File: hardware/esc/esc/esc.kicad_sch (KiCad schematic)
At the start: 17 parts, among them J1 JST SH 1.0mm, U10 TLV76733DRVR, U11 LMR51420YDDCR, U3 INA180B2

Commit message: redo layout and new board outline
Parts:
- C57, C58, C61, C62: footprint Capacitor_SMD:C_0603_1608Metric -> Capacitor_SMD:C_0402_1005Metric
- R21: footprint 3920:RES_3920R_1L00x_BRN -> Resistor_SMD:R_1206_3216Metric
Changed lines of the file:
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@@
 			)
 		)
-		(property "Footprint" "Capacitor_SMD:C_0603_1608Metric"
+		(property "Footprint" "Capacitor_SMD:C_0402_1005Metric"
 			(at 121.92 31.242 0)
 			(hide yes)
@@
 			)
 		)
-		(property "Footprint" "Capacitor_SMD:C_0603_1608Metric"
+		(property "Footprint" "Capacitor_SMD:C_0402_1005Metric"
 			(at 176.8348 49.53 0)
 			(hide yes)
@@
 			)
 		)
-		(property "Footprint" "Capacitor_SMD:C_0603_1608Metric"
+		(property "Footprint" "Capacitor_SMD:C_0402_1005Metric"
 			(at 90.4748 40.64 0)
 			(hide yes)
@@
 			)
 		)
-		(property "Footprint" "3920:RES_3920R_1L00x_BRN"
+		(property "Footprint" "Resistor_SMD:R_1206_3216Metric"
 			(at 27.432 35.56 90)
 			(hide yes)
@@
 			)
 		)
-		(property "Footprint" "Capacitor_SMD:C_0603_1608Metric"
+		(property "Footprint" "Capacitor_SMD:C_0402_1005Metric"
 			(at 212.3948 36.83 0)
 			(hide yes)

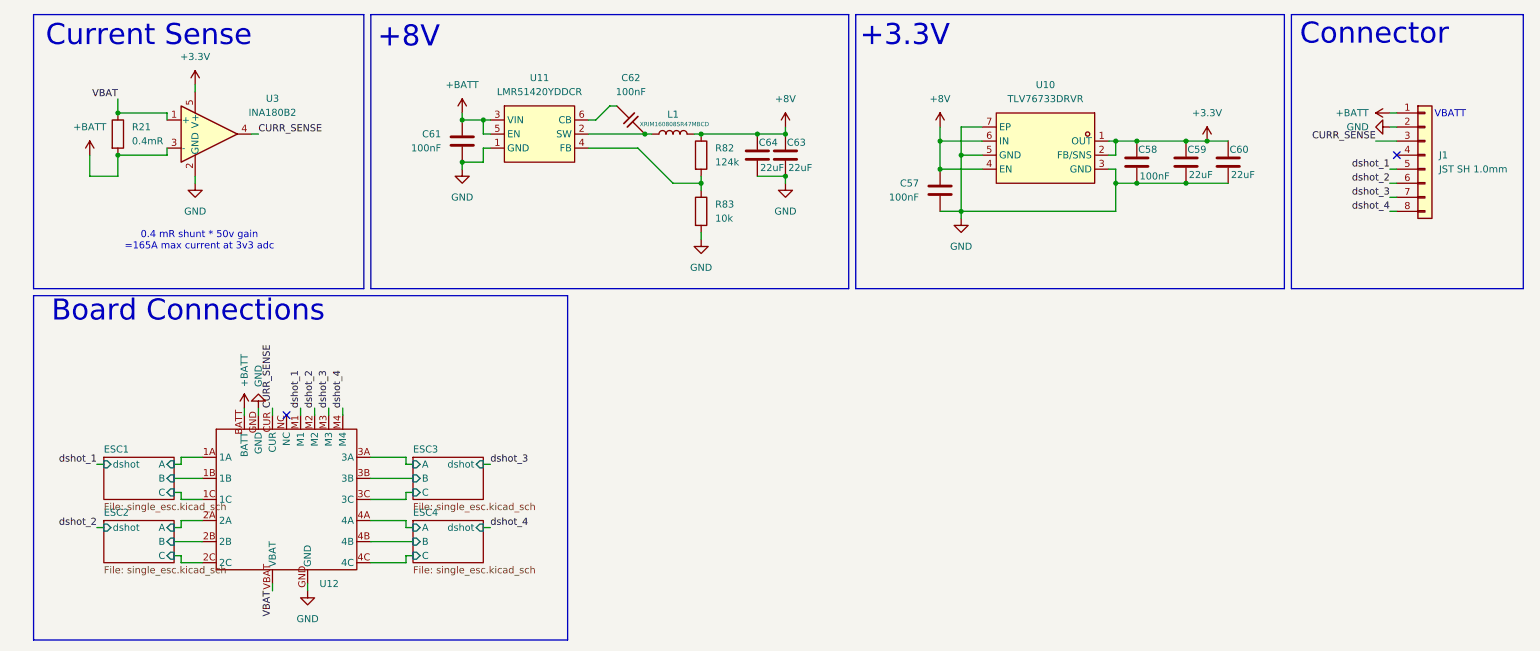
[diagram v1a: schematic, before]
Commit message: board pcb + res arrays
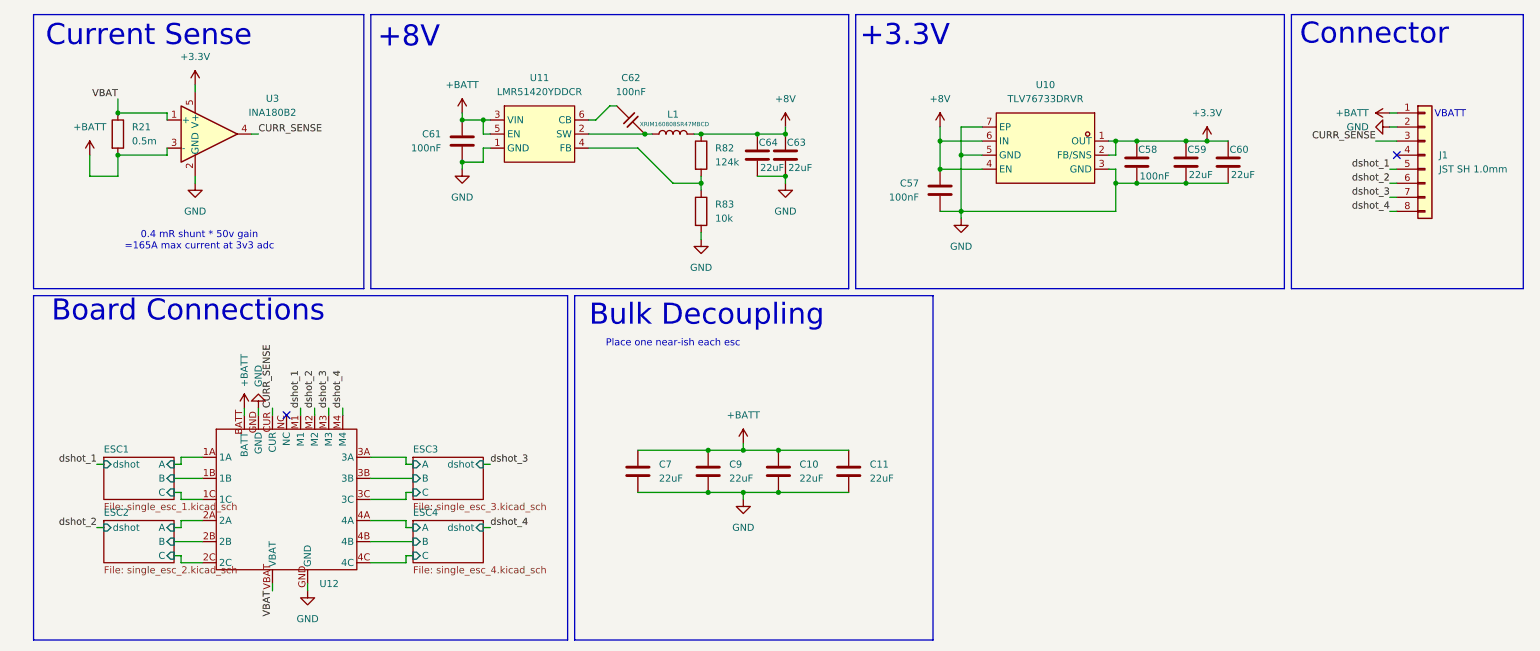
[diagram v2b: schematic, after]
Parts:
- added C10, C11, C7, C9: 22uF, Capacitor_SMD:C_0603_1608Metric, symbol Device:C
- R21: value 0.4mR -> 0.5m; footprint Resistor_SMD:R_1206_3216Metric -> bvn-z-r0005-1.0:BVNZR000510
- R83: footprint Resistor_SMD:R_0603_1608Metric -> Resistor_SMD:R_0402_1005Metric
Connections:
- net +BATT: now also C10.1, C11.1, C7.1, C9.1
- net GND: now also C10.2, C11.2, C7.2, C9.2
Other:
- sheet ESC1: file single_esc.kicad_sch -> single_esc_1.kicad_sch
- sheet ESC2: file single_esc.kicad_sch -> single_esc_2.kicad_sch
- sheet ESC3: file single_esc.kicad_sch -> single_esc_3.kicad_sch
- sheet ESC4: file single_esc.kicad_sch -> single_esc_4.kicad_sch
- note added: "Bulk Decoupling"
- note added: "Place one near-ish each esc"

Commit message: Routing done!
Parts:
- removed C60, C64: 22uF, Capacitor_SMD:C_0805_2012Metric, symbol Device:C
- added D4: LED, LED_SMD:LED_0603_1608Metric, symbol Device:LED
- added R64: 2.2k, Resistor_SMD:R_0402_1005Metric, symbol Device:R
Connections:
- net +3.3V: now also D4.2 (A)
- net GND: now also R64.2
- new net: D4.1 (K), R64.1
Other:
- moved on the sheet: C57, C58, C59, U10
